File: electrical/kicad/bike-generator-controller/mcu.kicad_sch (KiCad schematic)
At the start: 4 parts, among them J6 LiPo 1S / JST-PH 2.0 / PROV., U2 DFR0868 Beetle ESP32-C3

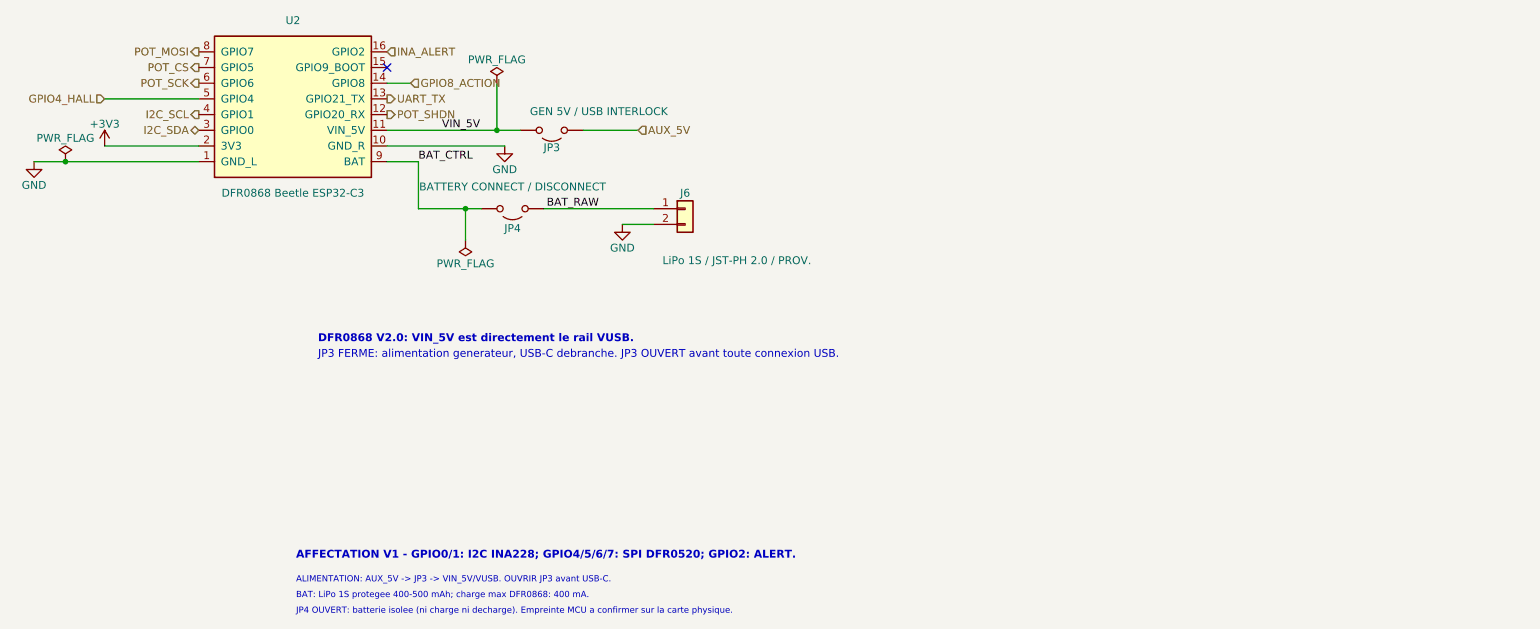
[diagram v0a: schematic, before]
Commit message: feat(controller): finalize V1 design and sourcing
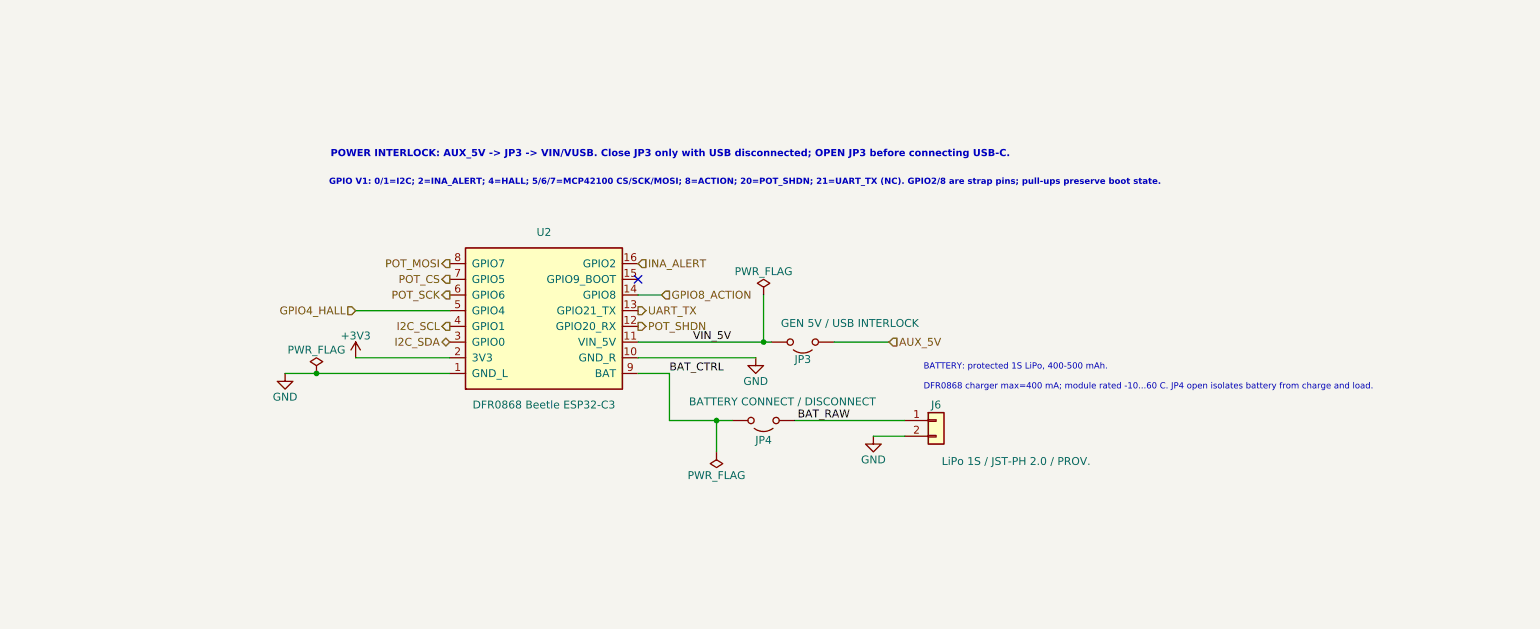
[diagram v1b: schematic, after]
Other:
- note added: "BATTERY: protected 1S LiPo, 400-500 mAh. DFR0868 charger max=400 mA; module rated -10...60 C. JP4 open isolates battery from charge and load."
- note added: "GPIO V1: 0/1=I2C; 2=INA_ALERT; 4=HALL; 5/6/7=MCP42100 CS/SCK/MOSI; 8=ACTION; 20=POT_SHDN; 21=UART_TX (NC). GPIO2/8 are strap pins; pull-ups preserve boot state."
- note added: "POWER INTERLOCK: AUX_5V -> JP3 -> VIN/VUSB. Close JP3 only with USB disconnected; OPEN JP3 before connecting USB-C."
- note removed: "AFFECTATION V1 - GPIO0/1: I2C INA228; GPIO4/5/6/7: SPI DFR0520; GPIO2: ALERT."
- note removed: "ALIMENTATION: AUX_5V -> JP3 -> VIN_5V/VUSB. OUVRIR JP3 avant USB-C."
- note removed: "BAT: LiPo 1S protegee 400-500 mAh; charge max DFR0868: 400 mA."
- note removed: "DFR0868 V2.0: VIN_5V est directement le rail VUSB."
- note removed: "JP3 FERME: alimentation generateur, USB-C debranche. JP3 OUVERT avant toute connexion USB."
- note removed: "JP4 OUVERT: batterie isolee (ni charge ni decharge). Empreinte MCU a confirmer sur la carte physique."
- moved on the sheet: J6, JP3, JP4, U2
